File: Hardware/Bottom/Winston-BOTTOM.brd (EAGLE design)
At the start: 33 x 33 mm, 31 parts, among them U1 AD5242-SO16

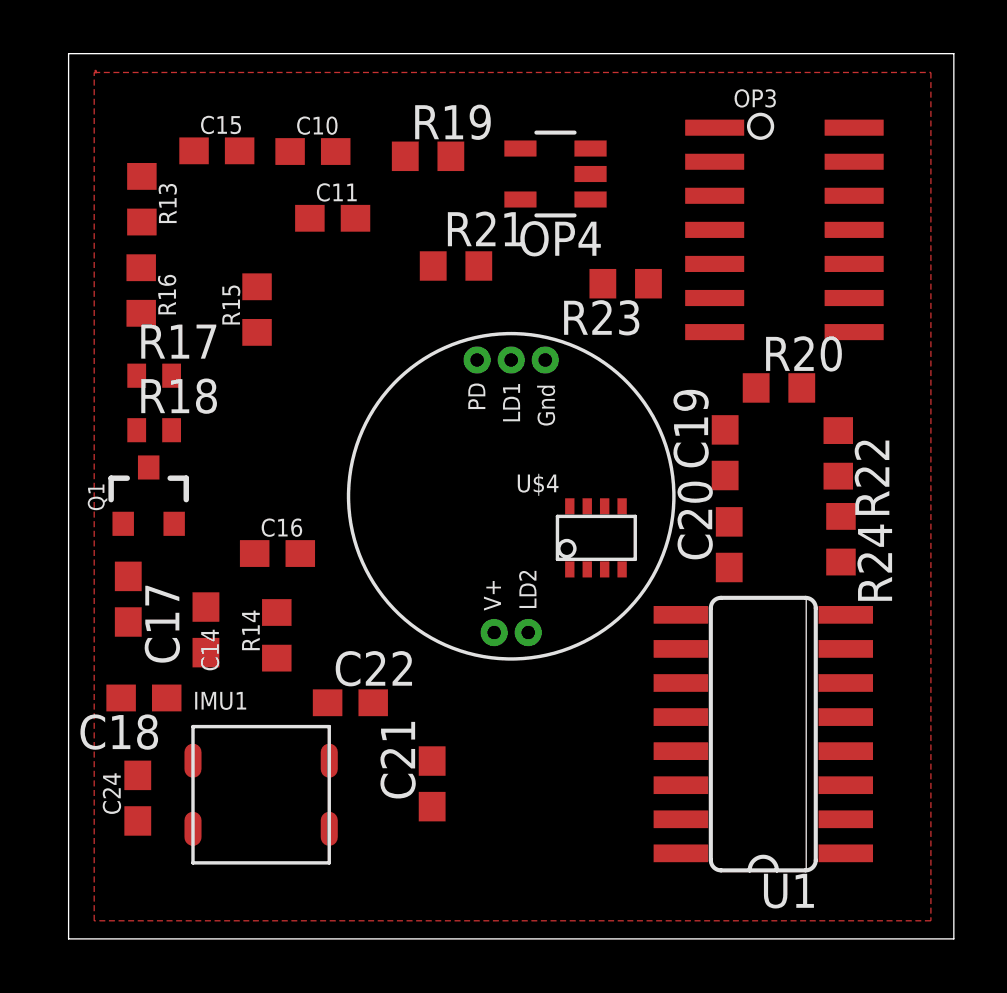
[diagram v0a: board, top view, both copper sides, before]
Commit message: updated top and bottom boards with everything from Take 002
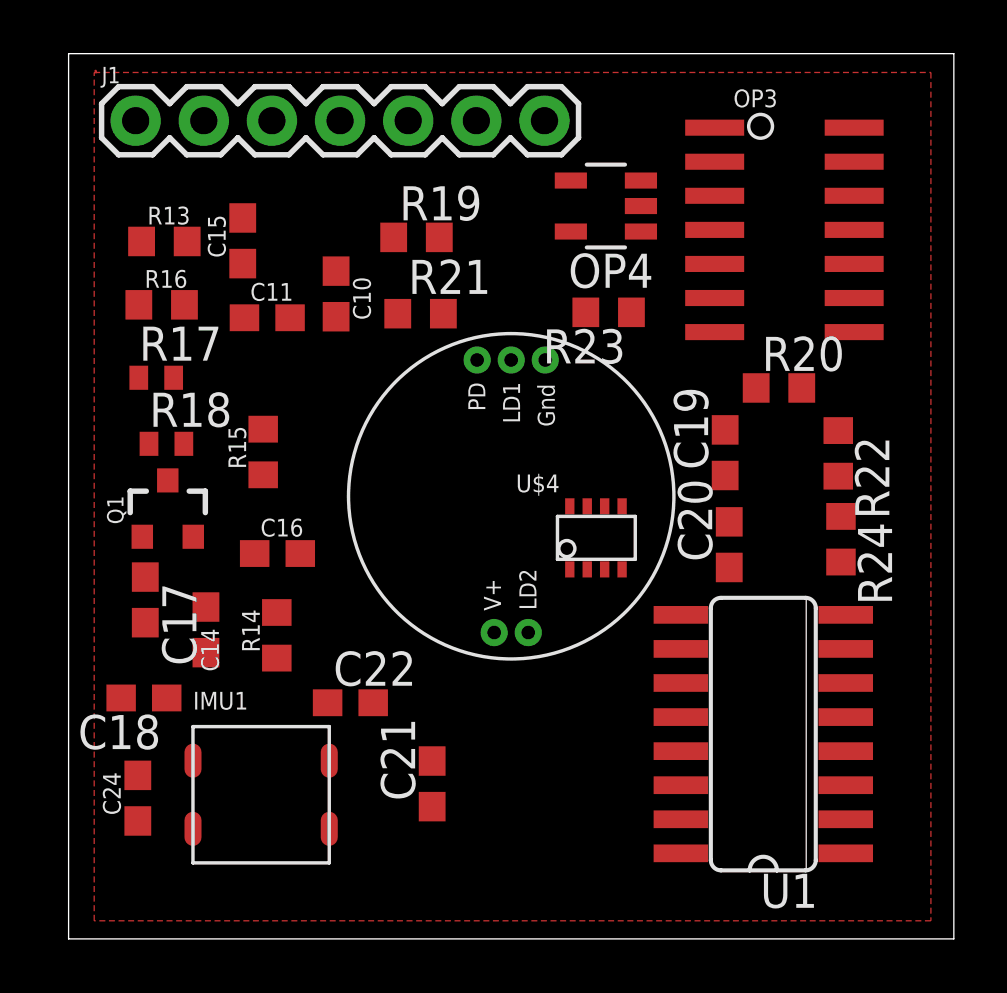
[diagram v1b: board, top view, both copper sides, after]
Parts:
- added J1: (no value), LinnesLab-Connectors:1X07
- moved C10 5.38 mm to (12.5, 26.5), turned to 270 degrees
- moved R15 5.31 mm to (9.75, 20.7)
- moved C11 4.44 mm to (9.91, 25.7)
- moved C15 3.49 mm to (8.99, 28.5), turned to 90 degrees
- moved R19 3.05 mm to (15.5, 28.7)
- moved OP4 2.23 mm to (22.5, 29.8)
- moved R21 2.21 mm to (15.6, 25.8)
- moved R13 1.78 mm to (6.07, 28.5), turned to 0 degrees
- moved R23 1.24 mm to (22.6, 25.9)
- moved R16 0.93 mm to (5.97, 26.1), turned to 0 degrees
- moved Q1 0.86 mm to (6.20, 18.5)
- moved R18 0.68 mm to (6.15, 21.0)
- moved C17 0.64 mm to (5.36, 15.1)
- moved R17 0.11 mm to (5.77, 23.4)
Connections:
- removed net LED.CTRL: U$4.8
- removed net PPG: C21.2, OP3.1, U1.14
- removed net TIA: C10.2, C15.1, OP4.1, U1.3
- new net A0/PPG: C21.2, J1.5, OP3.1, U1.14
- new net A7/TIA: C10.2, C15.1, J1.6, OP4.1, U1.3
- new net D29/LED.CTRL: J1.4, U$4.8
- new net N$11: J1.1
- new net N$6: J1.3
- new net N$7: J1.2

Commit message: finished routing all boards
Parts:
- removed J1: (no value), LinnesLab-Connectors:1X07
- added C1: 100n, LinnesLab-Passives:C0603
- added C2: 1u, LinnesLab-Passives:C0603
- added J2: (no value), LinnesLab-Connectors:1X07_1.27MM
- added U3: PCF8523, LinnesLab-Clocks:SO8
- added XTAL2: 32.7680kHz, LinnesLab-Clocks:2-SMD.NOLEAD.2.0MMTO1.2MM
- moved R13 33.0 mm to (32.6, 9.00), turned to 90 degrees
- moved C15 31.7 mm to (31.1, 5.72)
- moved R19 25.0 mm to (31.0, 8.98), turned to 270 degrees
- moved C11 23.3 mm to (24.1, 7.19), turned to 90 degrees
- moved C16 22.8 mm to (32.6, 12.5), turned to 90 degrees
- moved R15 22.6 mm to (30.8, 12.4), turned to 270 degrees
- moved R17 21.7 mm to (27.4, 21.7), turned to 90 degrees
- moved C14 21.3 mm to (27.6, 6.51), turned to 180 degrees
- moved IMU1 20.2 mm to (6.39, 27.8), turned to 90 degrees
- moved R18 20.0 mm to (26.1, 21.8), turned to 270 degrees
- moved R21 19.6 mm to (32.5, 15.9), turned to 270 degrees
- moved R14 18.2 mm to (27.5, 8.09), turned to 0 degrees
- moved R20 18.2 mm to (27.4, 4.95), turned to 180 degrees
- moved OP3 16.7 mm to (24.7, 12.8), turned to 0 degrees
- moved U1 16.6 mm to (11.8, 9.32), turned to 270 degrees
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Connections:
- removed net LED: Q1.3
- removed net N$11: J1.1
- removed net N$6: J1.3
- removed net N$7: J1.2
- new net N$1: U3.2, XTAL2.P$1
- new net N$2: U3.1, XTAL2.P$2
- new net VBATT: U3.3
- net 3.3V: now also C2.1, J2.4, U3.8
- net A0/PPG: now also J2.7; no longer J1.5
- net A7/TIA: now also J2.6; no longer J1.6
- net D29/LED.CTRL: now also J2.5; no longer J1.4
- net GND: now also C1.1, C2.2, J2.3, U3.4
- net LED.C: now also Q1.3
- net SCL: now also J2.2, U3.6
- net SDA: now also J2.1, U3.5
- net VREF: now also C1.2
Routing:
- net A7/TIA: track 0.00 -> 82.3 mm, vias 0 -> 4
- net SCL: track 0.00 -> 68.7 mm, vias 0 -> 6
- net SDA: track 0.00 -> 65.8 mm, vias 0 -> 4
- net A0/PPG: track 0.00 -> 45.8 mm
- net VREF: track 0.00 -> 42.4 mm, vias 0 -> 5
- net GND: track 0.00 -> 34.0 mm, vias 0 -> 14
- net PD.C: track 0.00 -> 24.6 mm, vias 0 -> 2
- net N$19: track 0.00 -> 21.5 mm
- net D29/LED.CTRL: track 0.00 -> 19.6 mm, vias 0 -> 2
- net N$9: track 0.00 -> 14.6 mm
- net G.W2: track 0.00 -> 14.5 mm, vias 0 -> 2
- net N$17: track 0.00 -> 10.9 mm, vias 0 -> 2
- net N$13: track 0.00 -> 10.9 mm, vias 0 -> 2
- net N$10: track 0.00 -> 8.58 mm
- net N$16: track 0.00 -> 8.45 mm
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- added copper zone on layer 16, net GND
- removed copper zone on layer 1, net N$1
